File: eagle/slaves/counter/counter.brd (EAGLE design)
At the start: 126.2 x 32 mm, 76 parts, among them IC1 MCP1703DB, IC2 4067D, IC3 74HC154DW, J1 RJ12RIGHTANGLE-I2C, X2 8MHz, X4 MINI-USB

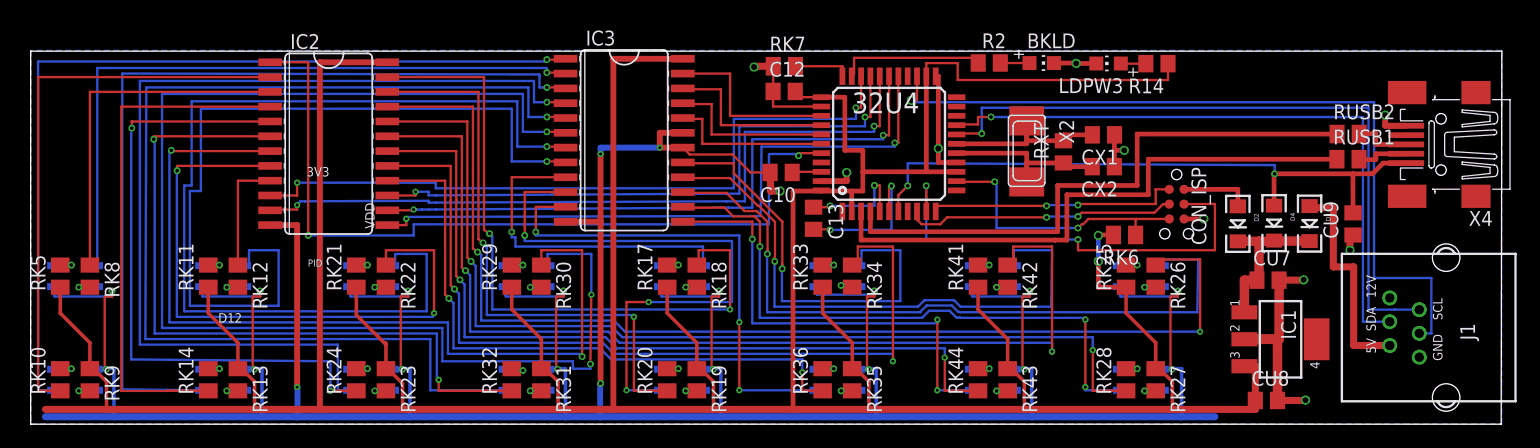
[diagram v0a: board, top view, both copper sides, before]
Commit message: increasing IR detector pad size
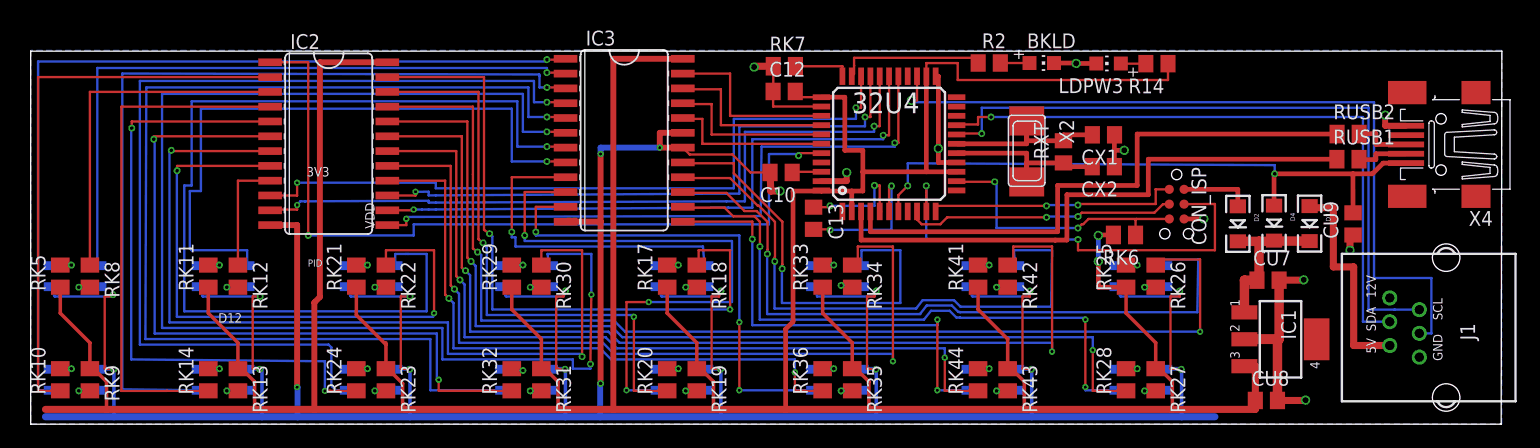
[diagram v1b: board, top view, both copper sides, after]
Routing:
- net DMUX3: track 70.4 -> 55.5 mm
- net GND: track 391.6 -> 399.2 mm
